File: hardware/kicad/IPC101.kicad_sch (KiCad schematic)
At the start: 13 parts, among them J1 IPC-100 J10, J3 IPC-100 J8A STOP, SW1 START B3F-4055, SW2 PULL B3F-4055, SW3 ADAFRUIT 504 - VERIFY PIN MAP, U1 TCA8418RTWR

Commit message: Complete routed IPC-101 Rev C control board
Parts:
- added D1: RGB COMMON ANODE 5MM, IPC101:LED_RGB_5MM_CA, symbol IPC101:LED_RGB_CA
- added R2: 1k RED, IPC101:R0805, symbol IPC101:R
- added R3: 1k GREEN, IPC101:R0805, symbol IPC101:R
- added R4: 1k BLUE, IPC101:R0805, symbol IPC101:R
- SW1: value START B3F-4055 -> ARM B3F-4055
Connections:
- net +3V3: now also D1.2 (A); no longer U1.12 (COL3), U1.13 (COL4), U1.14 (COL5)
- net R5_START renamed R5_ARM
- new net RGB_B_GPIO: R4.2, U1.12 (COL3)
- new net RGB_B_K: D1.1 (R_K), R4.1
- new net RGB_G_GPIO: R3.2, U1.13 (COL4)
- new net RGB_G_K: D1.3 (G_K), R3.1
- new net RGB_R_GPIO: R2.2, U1.14 (COL5)
- new net RGB_R_K: D1.4 (B_K), R2.1
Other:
- note added: "DS1 Hosyond 2.42-inch SSD1309 OLED mounts to the faceplate and uses a dedicated 5-wire harness to IPC-100 J6: OLED_VCC, GND, SDA, SCL, RESET."
- note added: "U1 COL6/COL7/COL8 are RGB GPIO sinks through 1k resistors; remaining unused matrix pins are held at +3V3."
- note removed: "DS1 Hosyond 2.42-inch SSD1309 OLED is mounted on IPC-101 and uses a dedicated 5-wire harness to IPC-100 J6: OLED_VCC, GND, SDA, SCL, RESET."
- note removed: "U1 unused ROW7/COL1..COL9 held at +3V3 for defined reset state. Review whether 100 kΩ series pull-ups are required before PCB release."
- title: IPC-101 P0 Operator Control Panel -> IPC-101 Rev C Operator Control Panel
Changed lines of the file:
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@@
 (kicad_sch (version 20231120) (generator eeschema)
   (paper "A4")
-  (title_block (title "IPC-101 P0 Operator Control Panel") (date "2026-09-01") (rev "P0") (company "Iron Pine Outdoors") (comment 1 "Connected engineering schematic — fabrication hold") (comment 2 "SW3 footprint/pin map and U1 land pattern require physical verification"))
+  (title_block (title "IPC-101 Rev C Operator Control Panel") (date "2026-09-03") (rev "C") (company "Iron Pine Outdoors") (comment 1 "Crosswind replacement control-panel core") (comment 2 "OLED left / navigation right / ARM and PULL / onboard RGB"))
   (text "IPC-100 J10 — 3.3 V / 100 kHz I2C / NO LOCAL BUS PULL-UPS" (at 20 20 0) (effects (font (size 1.27 1.27) (bold yes)) (justify left bottom)))
-  (text "U1 unused ROW7/COL1..COL9 held at +3V3 for defined reset state. Review whether 100 kΩ series pull-ups are required before PCB release." (at 80 120 0) (effects (font (size 1 1) (italic yes)) (justify left bottom)))
+  (text "U1 COL6/COL7/COL8 are RGB GPIO sinks through 1k resistors; remaining unused matrix pins are held at +3V3." (at 80 120 0) (effects (font (size 1 1) (italic yes)) (justify left bottom)))
   (text "SAFETY STOP: J3 is IPC-100 J8A only. Neither pin connects to logic GND or +3V3." (at 20 175 0) (effects (font (size 1.27 1.27) (bold yes)) (justify left bottom)))
-  (text "DS1 Hosyond 2.42-inch SSD1309 OLED is mounted on IPC-101 and uses a dedicated 5-wire harness to IPC-100 J6: OLED_VCC, GND, SDA, SCL, RESET." (at 20 190 0) (effects (font (size 1 1)) (justify left bottom)))
+  (text "DS1 Hosyond 2.42-inch SSD1309 OLED mounts to the faceplate and uses a dedicated 5-wire harness to IPC-100 J6: OLED_VCC, GND, SDA, SCL, RESET." (at 20 190 0) (effects (font (size 1 1)) (justify left bottom)))
   (symbol (lib_id "IPC101:CONN4") (at 35 35 0) (unit 1) (exclude_from_sim no) (in_bom yes) (on_board yes) (dnp no)
     (property "Reference" "J1" (at 35 27 0) (effects (font (size 1 1)))) (property "Value" "IPC-100 J10" (at 35 43 0) (effects (font (size 1 1)))) (property "Footprint" "IPC101:JST_GH_04" (at 35 35 0) (effects (font (size 1 1)) hide)) (property "Datasheet" "https://www.jst-mfg.com/product/pdf/eng/eGH.pdf" (at 35 35 0) (effects (font (size 1 1)) hide))
@@
   (label "+3V3" (at 87.22 97.86 180) (effects (font (size .9 .9)) (justify right bottom)))
   (label "R6_PULL" (at 87.22 92.78 180) (effects (font (size .9 .9)) (justify right bottom)))
-  (label "R5_START" (at 87.22 87.7 180) (effects (font (size .9 .9)) (justify right bottom)))
+  (label "R5_ARM" (at 87.22 87.7 180) (effects (font (size .9 .9)) (justify right bottom)))
   (label "R4_SELECT" (at 87.22 82.62 180) (effects (font (size .9 .9)) (justify right bottom)))
   (label "R3_DOWN" (at 87.22 77.54 180) (effects (font (size .9 .9)) (justify right bottom)))
@@
   (label "+3V3" (at 122.78 52.14 0) (effects (font (size .9 .9)) (justify left bottom)))
   (label "+3V3" (at 122.78 57.22 0) (effects (font (size .9 .9)) (justify left bottom)))
-  (label "+3V3" (at 122.78 62.3 0) (effects (font (size .9 .9)) (justify left bottom)))
-  (label "+3V3" (at 122.78 67.38 0) (effects (font (size .9 .9)) (justify left bottom)))
+  (label "RGB_B_GPIO" (at 122.78 62.3 0) (effects (font (size .9 .9)) (justify left bottom)))
+  (label "RGB_G_GPIO" (at 122.78 67.38 0) (effects (font (size .9 .9)) (justify left bottom)))
   (label "+3V3" (at 122.78 77.54 0) (effects (font (size .9 .9)) (justify left bottom)))
-  (label "+3V3" (at 122.78 72.46 0) (effects (font (size .9 .9)) (justify left bottom)))
+  (label "RGB_R_GPIO" (at 122.78 72.46 0) (effects (font (size .9 .9)) (justify left bottom)))
   (label "+3V3" (at 122.78 82.62 0) (effects (font (size .9 .9)) (justify left bottom)))
   (label "+3V3" (at 122.78 87.7 0) (effects (font (size .9 .9)) (justify left bottom)))
@@
   (label "R4_SELECT" (at 34 73.65 180) (effects (font (size .9 .9)) (justify right bottom)))
   (symbol (lib_id "IPC101:SW2") (at 45 105 0) (unit 1) (exclude_from_sim no) (in_bom yes) (on_board yes) (dnp no)
-    (property "Reference" "SW1" (at 45 101 0) (effects (font (size 1 1)))) (property "Value" "START B3F-4055" (at 45 109 0) (effects (font (size 1 1)))) (property "Footprint" "IPC101:B3F-4055" (at 45 105 0) (effects (font (size 1 1)) hide)) (property "Datasheet" "https://components.omron.com/us-en/datasheet_pdf/A070-E1.pdf" (at 45 105 0) (effects (font (size 1 1)) hide)) (pin "1") (pin "2") (instances (project "IPC101" (path "/10100000-0000-4000-8000-000000000200" (reference "SW1") (unit 1)))))
-  (label "R5_START" (at 37.38 105 180) (effects (font (size .9 .9)) (justify right bottom)))
+    (property "Reference" "SW1" (at 45 101 0) (effects (font (size 1 1)))) (property "Value" "ARM B3F-4055" (at 45 109 0) (effects (font (size 1 1)))) (property "Footprint" "IPC101:B3F-4055" (at 45 105 0) (effects (font (size 1 1)) hide)) (property "Datasheet" "https://components.omron.com/us-en/datasheet_pdf/A070-E1.pdf" (at 45 105 0) (effects (font (size 1 1)) hide)) (pin "1") (pin "2") (instances (project "IPC101" (path "/10100000-0000-4000-8000-000000000200" (reference "SW1") (unit 1)))))
+  (label "R5_ARM" (at 37.38 105 180) (effects (font (size .9 .9)) (justify right bottom)))
   (label "C0" (at 52.62 105 0) (effects (font (size .9 .9)) (justify left bottom)))
   (symbol (lib_id "IPC101:SW2") (at 45 120 0) (unit 1) (exclude_from_sim no) (in_bom yes) (on_board yes) (dnp no)
@@
   (symbol (lib_id "IPC101:TP") (at 190 75 0) (unit 1) (exclude_from_sim no) (in_bom yes) (on_board yes) (dnp no) (property "Reference" "TP4" (at 190 72 0) (effects (font (size 1 1)))) (property "Value" "SCL" (at 190 78 0) (effects (font (size .8 .8)))) (property "Footprint" "IPC101:TEST_LOOP" (at 190 75 0) (effects (font (size 1 1)) hide)) (property "Datasheet" "" (at 190 75 0) (effects (font (size 1 1)) hide)) (pin "1") (instances (project "IPC101" (path "/10100000-0000-4000-8000-000000000290" (reference "TP4") (unit 1)))))
   (label "SCL" (at 184.92 75 180) (effects (font (size .9 .9)) (justify right bottom)))
+  (symbol (lib_id "IPC101:R") (at 145 135 0) (unit 1) (exclude_from_sim no) (in_bom yes) (on_board yes) (dnp no) (property "Reference" "R2" (at 147 135 90) (effects (font (size 1 1)))) (property "Value" "1k RED" (at 142 135 90) (effects (font (size 1 1)))) (property "Footprint" "IPC101:R0805" (at 145 135 0) (effects (font (size 1 1)) hide)) (property "Datasheet" "" (at 145 135 0) (effects (font (size 1 1)) hide)) (pin "1") (pin "2") (instances (project "IPC101" (path "/10100000-0000-4000-8000-000000000300" (reference "R2") (unit 1)))))
+  (label "RGB_R_GPIO" (at 145 129.92 90) (effects (font (size .9 .9)) (justify left bottom)))
+  (label "RGB_R_K" (at 145 140.08 270) (effects (font (size .9 .9)) (justify right bottom)))
+  (symbol (lib_id "IPC101:R") (at 160 135 0) (unit 1) (exclude_from_sim no) (in_bom yes) (on_board yes) (dnp no) (property "Reference" "R3" (at 162 135 90) (effects (font (size 1 1)))) (property "Value" "1k GREEN" (at 157 135 90) (effects (font (size 1 1)))) (property "Footprint" "IPC101:R0805" (at 160 135 0) (effects (font (size 1 1)) hide)) (property "Datasheet" "" (at 160 135 0) (effects (font (size 1 1)) hide)) (pin "1") (pin "2") (instances (project "IPC101" (path "/10100000-0000-4000-8000-000000000310" (reference "R3") (unit 1)))))
+  (label "RGB_G_GPIO" (at 160 129.92 90) (effects (font (size .9 .9)) (justify left bottom)))
+  (label "RGB_G_K" (at 160 140.08 270) (effects (font (size .9 .9)) (justify right bottom)))
+  (symbol (lib_id "IPC101:R") (at 175 135 0) (unit 1) (exclude_from_sim no) (in_bom yes) (on_board yes) (dnp no) (property "Reference" "R4" (at 177 135 90) (effects (font (size 1 1)))) (property "Value" "1k BLUE" (at 172 135 90) (effects (font (size 1 1)))) (property "Footprint" "IPC101:R0805" (at 175 135 0) (effects (font (size 1 1)) hide)) (property "Datasheet" "" (at 175 135 0) (effects (font (size 1 1)) hide)) (pin "1") (pin "2") (instances (project "IPC101" (path "/10100000-0000-4000-8000-000000000320" (reference "R4") (unit 1)))))
+  (label "RGB_B_GPIO" (at 175 129.92 90) (effects (font (size .9 .9)) (justify left bottom)))
+  (label "RGB_B_K" (at 175 140.08 270) (effects (font (size .9 .9)) (justify right bottom)))
+  (symbol (lib_id "IPC101:LED_RGB_CA") (at 180 155 0) (unit 1) (exclude_from_sim no) (in_bom yes) (on_board yes) (dnp no) (property "Reference" "D1" (at 180 149 0) (effects (font (size 1 1)))) (property "Value" "RGB COMMON ANODE 5MM" (at 180 161 0) (effects (font (size 1 1)))) (property "Footprint" "IPC101:LED_RGB_5MM_CA" (at 180 155 0) (effects (font (size 1 1)) hide)) (property "Datasheet" "" (at 180 155 0) (effects (font (size 1 1)) hide)) (pin "1") (pin "2") (pin "3") (pin "4") (instances (project "IPC101" (path "/10100000-0000-4000-8000-000000000330" (reference "D1") (unit 1)))))
+  (label "RGB_R_K" (at 172 152.46 180) (effects (font (size .9 .9)) (justify right bottom)))
+  (label "RGB_G_K" (at 172 155 180) (effects (font (size .9 .9)) (justify right bottom)))
+  (label "RGB_B_K" (at 172 157.54 180) (effects (font (size .9 .9)) (justify right bottom)))
+  (label "+3V3" (at 188 155 0) (effects (font (size .9 .9)) (justify left bottom)))
   (sheet_instances (path "/" (page "1")))
 )

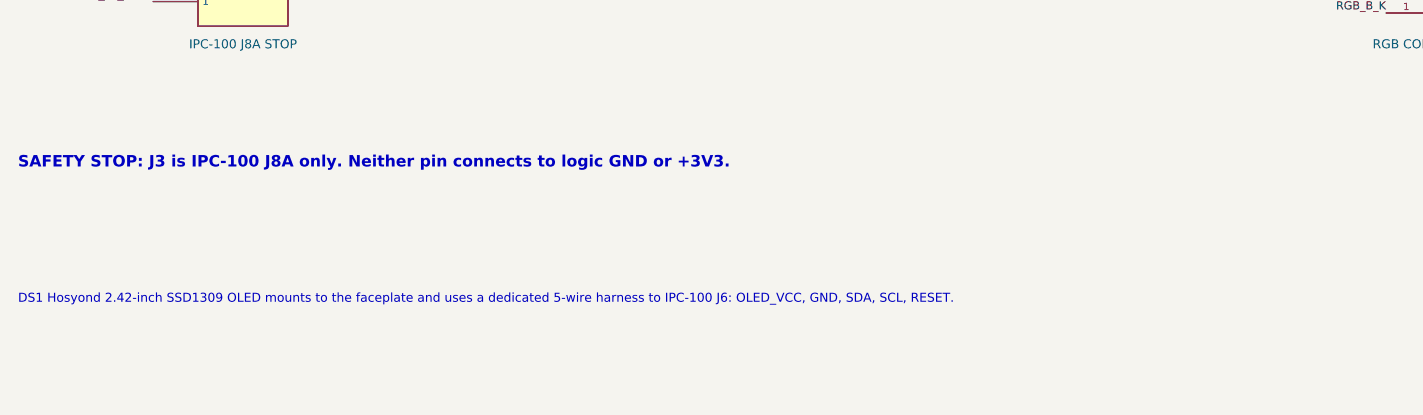
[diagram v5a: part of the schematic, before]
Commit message: Route OLED harness through IPC-101
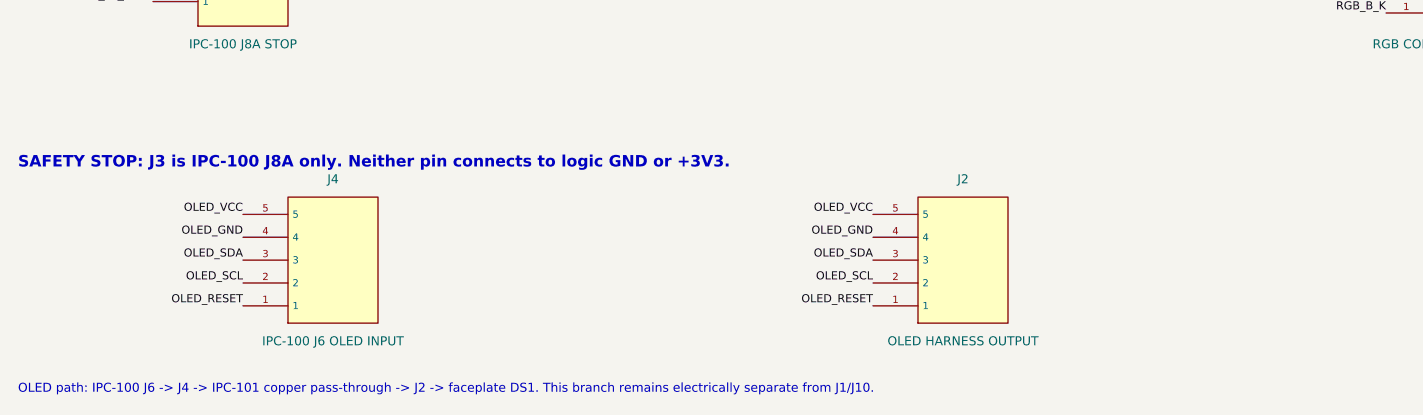
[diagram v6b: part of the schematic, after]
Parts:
- added J2: OLED HARNESS OUTPUT, Connector_JST:JST_XH_B5B-XH-A_1x05_P2.50mm_Vertical, symbol IPC101:CONN5
- added J4: IPC-100 J6 OLED INPUT, Connector_JST:JST_GH_SM05B-GHS-TB_1x05-1MP_P1.25mm_Horizontal, symbol IPC101:CONN5
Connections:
- new net OLED_GND: J2.4, J4.4
- new net OLED_RESET: J2.1, J4.1
- new net OLED_SCL: J2.2, J4.2
- new net OLED_SDA: J2.3, J4.3
- new net OLED_VCC: J2.5, J4.5
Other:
- note added: "OLED path: IPC-100 J6 -> J4 -> IPC-101 copper pass-through -> J2 -> faceplate DS1. This branch remains electrically separate from J1/J10."
- note removed: "DS1 Hosyond 2.42-inch SSD1309 OLED mounts to the faceplate and uses a dedicated 5-wire harness to IPC-100 J6: OLED_VCC, GND, SDA, SCL, RESET."
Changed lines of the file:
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@@
   (text "U1 COL6/COL7/COL8 are RGB GPIO sinks through 1k resistors; remaining unused matrix pins are held at +3V3." (at 80 120 0) (effects (font (size 1 1) (italic yes)) (justify left bottom)))
   (text "SAFETY STOP: J3 is IPC-100 J8A only. Neither pin connects to logic GND or +3V3." (at 20 175 0) (effects (font (size 1.27 1.27) (bold yes)) (justify left bottom)))
-  (text "DS1 Hosyond 2.42-inch SSD1309 OLED mounts to the faceplate and uses a dedicated 5-wire harness to IPC-100 J6: OLED_VCC, GND, SDA, SCL, RESET." (at 20 190 0) (effects (font (size 1 1)) (justify left bottom)))
+  (text "OLED path: IPC-100 J6 -> J4 -> IPC-101 copper pass-through -> J2 -> faceplate DS1. This branch remains electrically separate from J1/J10." (at 20 200 0) (effects (font (size 1 1)) (justify left bottom)))
   (symbol (lib_id "IPC101:CONN4") (at 35 35 0) (unit 1) (exclude_from_sim no) (in_bom yes) (on_board yes) (dnp no)
     (property "Reference" "J1" (at 35 27 0) (effects (font (size 1 1)))) (property "Value" "IPC-100 J10" (at 35 43 0) (effects (font (size 1 1)))) (property "Footprint" "IPC101:JST_GH_04" (at 35 35 0) (effects (font (size 1 1)) hide)) (property "Datasheet" "https://www.jst-mfg.com/product/pdf/eng/eGH.pdf" (at 35 35 0) (effects (font (size 1 1)) hide))
@@
   (label "RGB_B_K" (at 172 157.54 180) (effects (font (size .9 .9)) (justify right bottom)))
   (label "+3V3" (at 188 155 0) (effects (font (size .9 .9)) (justify left bottom)))
+  (symbol (lib_id "IPC101:CONN5") (at 55 185 0) (unit 1) (exclude_from_sim no) (in_bom yes) (on_board yes) (dnp no) (property "Reference" "J4" (at 55 176 0) (effects (font (size 1 1)))) (property "Value" "IPC-100 J6 OLED INPUT" (at 55 194 0) (effects (font (size 1 1)))) (property "Footprint" "Connector_JST:JST_GH_SM05B-GHS-TB_1x05-1MP_P1.25mm_Horizontal" (at 55 185 0) (effects (font (size 1 1)) hide)) (property "Datasheet" "https://www.jst-mfg.com/product/pdf/eng/eGH.pdf" (at 55 185 0) (effects (font (size 1 1)) hide)) (pin "1") (pin "2") (pin "3") (pin "4") (pin "5") (instances (project "IPC101" (path "/10100000-0000-4000-8000-000000000340" (reference "J4") (unit 1)))))
+  (label "OLED_VCC" (at 45 179.92 180) (effects (font (size .9 .9)) (justify right bottom)))
+  (label "OLED_GND" (at 45 182.46 180) (effects (font (size .9 .9)) (justify right bottom)))
+  (label "OLED_SDA" (at 45 185 180) (effects (font (size .9 .9)) (justify right bottom)))
+  (label "OLED_SCL" (at 45 187.54 180) (effects (font (size .9 .9)) (justify right bottom)))
+  (label "OLED_RESET" (at 45 190.08 180) (effects (font (size .9 .9)) (justify right bottom)))
+  (symbol (lib_id "IPC101:CONN5") (at 125 185 0) (unit 1) (exclude_from_sim no) (in_bom yes) (on_board yes) (dnp no) (property "Reference" "J2" (at 125 176 0) (effects (font (size 1 1)))) (property "Value" "OLED HARNESS OUTPUT" (at 125 194 0) (effects (font (size 1 1)))) (property "Footprint" "Connector_JST:JST_XH_B5B-XH-A_1x05_P2.50mm_Vertical" (at 125 185 0) (effects (font (size 1 1)) hide)) (property "Datasheet" "https://www.jst-mfg.com/product/pdf/eng/eXH.pdf" (at 125 185 0) (effects (font (size 1 1)) hide)) (pin "1") (pin "2") (pin "3") (pin "4") (pin "5") (instances (project "IPC101" (path "/10100000-0000-4000-8000-000000000360" (reference "J2") (unit 1)))))
+  (label "OLED_VCC" (at 115 179.92 180) (effects (font (size .9 .9)) (justify right bottom)))
+  (label "OLED_GND" (at 115 182.46 180) (effects (font (size .9 .9)) (justify right bottom)))
+  (label "OLED_SDA" (at 115 185 180) (effects (font (size .9 .9)) (justify right bottom)))
+  (label "OLED_SCL" (at 115 187.54 180) (effects (font (size .9 .9)) (justify right bottom)))
+  (label "OLED_RESET" (at 115 190.08 180) (effects (font (size .9 .9)) (justify right bottom)))
   (sheet_instances (path "/" (page "1")))
 )
